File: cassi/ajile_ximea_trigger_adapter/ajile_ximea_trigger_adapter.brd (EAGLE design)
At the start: 50.8 x 81 mm, 10 parts, among them K1 694108105102

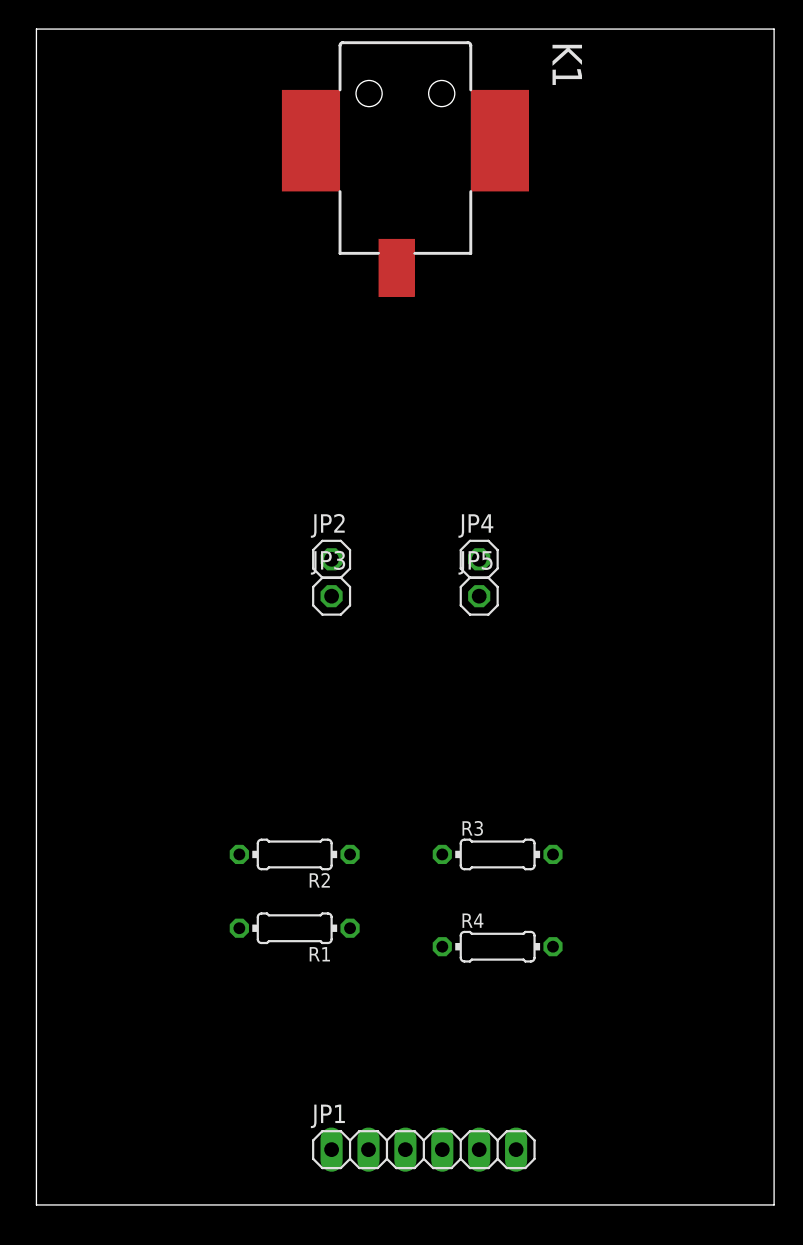
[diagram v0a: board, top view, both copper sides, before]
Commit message: finished trigger adapter board
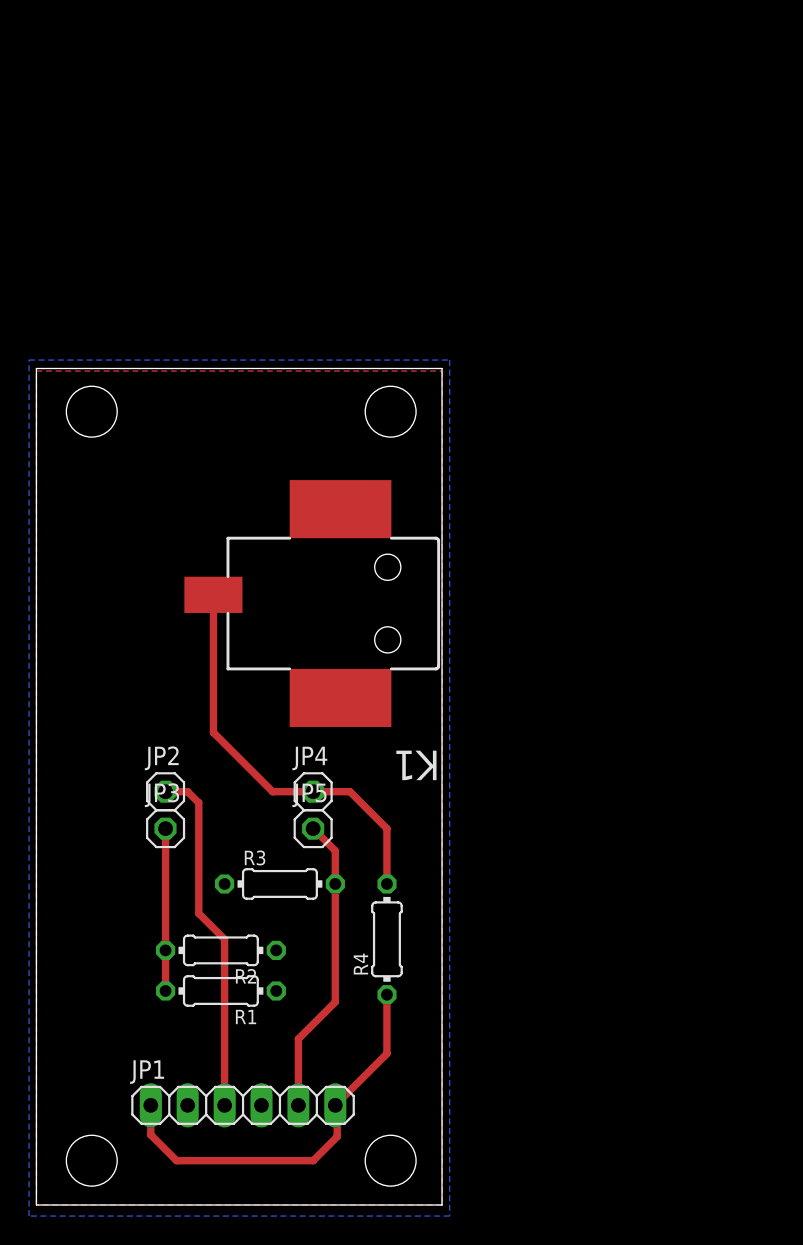
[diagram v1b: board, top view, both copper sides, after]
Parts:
- moved K1 38.7 mm to (27.7, 41.4), turned to 180 degrees
- moved JP2 19.7 mm to (8.89, 28.4)
- moved JP4 19.7 mm to (19.1, 28.4)
- moved JP3 19.7 mm to (8.89, 25.9)
- moved JP5 19.7 mm to (19.1, 25.9)
- moved R3 15.1 mm to (16.8, 22.1)
- moved JP1 12.8 mm to (14.2, 6.86)
- moved R2 8.33 mm to (12.7, 17.5)
- moved R4 7.64 mm to (24.1, 18.3), turned to 90 degrees
- moved R1 6.67 mm to (12.7, 14.7)
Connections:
- removed net XIMEA_OUT: JP1.6, R4.1
- net AJILE_IN: now also JP1.6, R4.1
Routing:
- net 5V: track 0.00 -> 28.0 mm
- net AJILE_IN: track 0.00 -> 27.7 mm
- net AJILE_OUT: track 0.00 -> 24.2 mm
- net XIMEA_IN: track 0.00 -> 20.7 mm
- net N$2: track 0.00 -> 11.2 mm
- added copper zone on layer 1, net GND
- added copper zone on layer 16, net GND
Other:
- board size 50.8 x 81 mm -> 27.9 x 57.6 mm
